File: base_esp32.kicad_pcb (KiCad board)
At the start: 2 copper layers, 100 x 100 mm, 104 parts, among them J1 H_Src_raw, J10 S_IO, J11 H_KEYPAD, J12 S_KEYPAD, J13 BYPASS SRC 5V, J14 BYPASS SRC 3V3, J15 H_SERVO, J16 H_INA1, J17 H_BUZZER, J18 H_INB1, J19 H_IO34, J2 H_5V, J20 H_I2C, J21 S_I2C, J22 H_IO35, J23 H_INA2, J24 H_INB2, J25 H_IO36, J26 H_SPI, J27 S_SPI, J28 DTH11_V1, J29 DTH11_V2, J3 S_5V, J30 H_DTH11, J31 H_DS18B, J32 H_IO39, J33 TX_RX, J34 MOTOR, J35 H_TRIGGER, J36 H_IO33_OUT, J37 H_IO33, J38 ULTRASONIC, J39 H_IO15, J4 H_3V3_2, J40 H_IO15_OUT, J41 H_ECHO, J42 H_IO32, J43 H_IO32_OUT, J44 H_IO02, J45 H_IO02_OUT, J46 H_IO04, J47 H_IO04_OUT, J5 S_3V3_2, J6 H_GND, J7 S_GND, J8 Input Source, J9 H_IO, M1 Servo, SW1 SW_DIP_KEYPAD_1, SW2 SW_DIP_KEYPAD_2, SW3 ENABLE, SW4 INPUT_D1, SW5 SW_DIP_INPUTS, SW6 INPUT_D2, SW7 Selector Input 1, SW8 Selector Input 2, U1 LM7805_TO220, U2 AMS1117, U3 ESP32-DEVKIT-V1, U4 AMS1117, U5 MX1508, U6 DS18B20, U7 LM35-LP

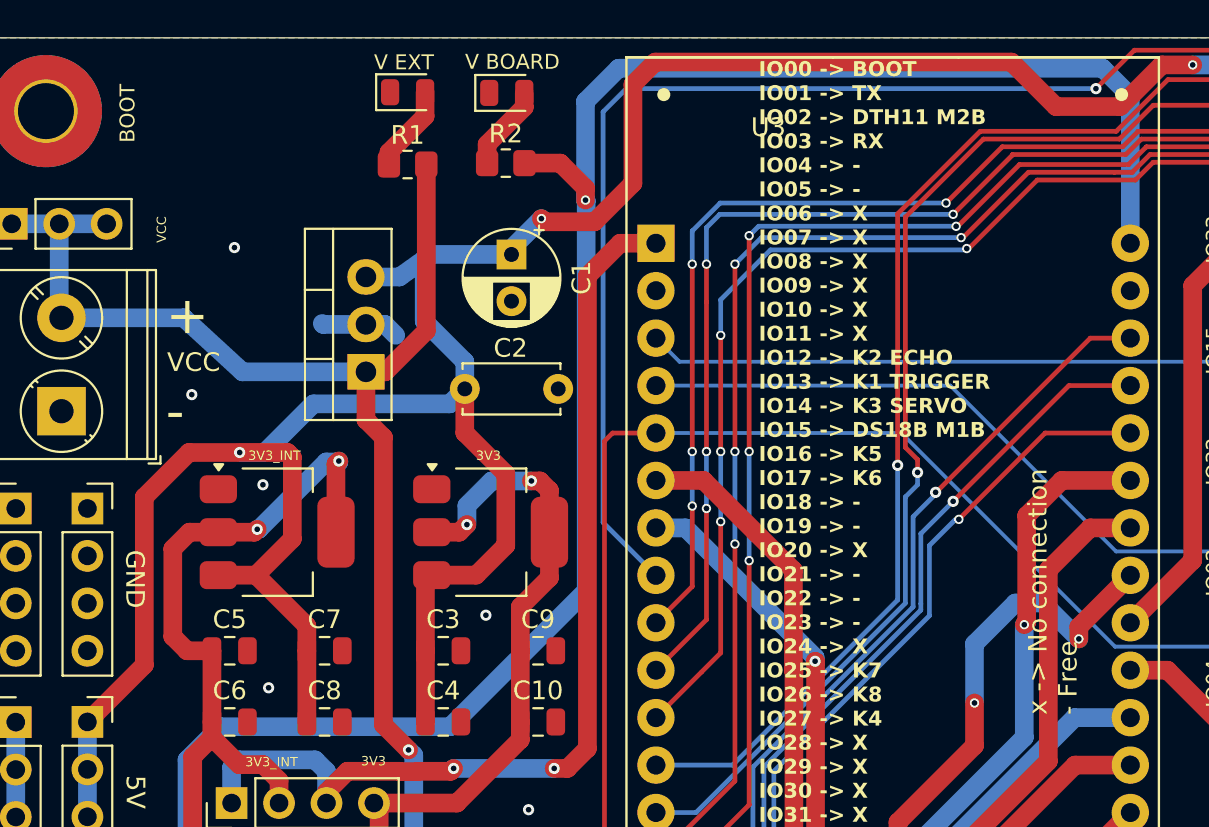
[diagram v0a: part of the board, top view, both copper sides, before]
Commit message: fix: f silkscreen
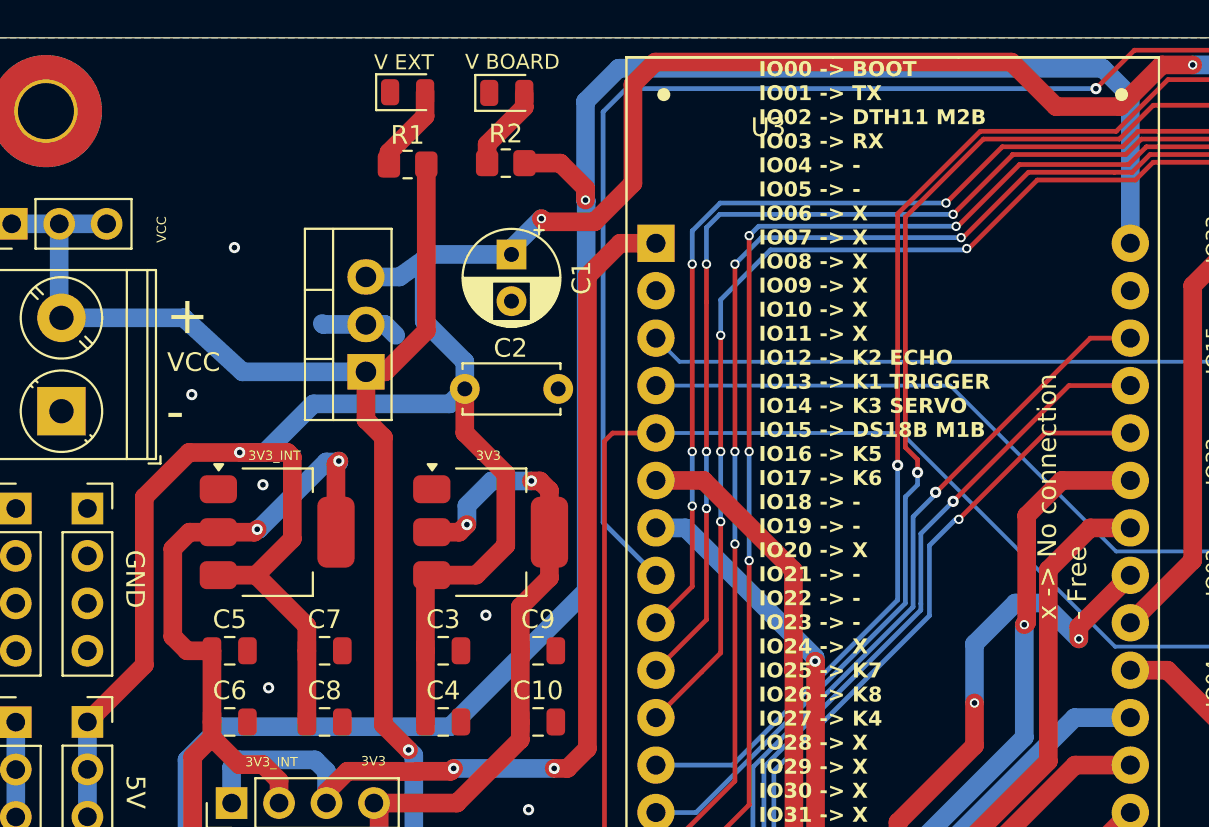
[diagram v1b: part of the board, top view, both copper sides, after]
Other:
- board text removed: "BOOT"
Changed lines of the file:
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@@
 		(pcbplotparams
 			(layerselection 0x00010fc_ffffffff)
-			(plot_on_all_layers_selection 0x0000000_00000000)
+			(plot_on_all_layers_selection 0x0001000_00000000)
 			(disableapertmacros no)
 			(usegerberextensions yes)
@@
 			(sketchpadsonfab no)
 			(subtractmaskfromsilk yes)
-			(outputformat 1)
+			(outputformat 4)
 			(mirror no)
-			(drillshape 0)
+			(drillshape 2)
 			(scaleselection 1)
-			(outputdirectory "gerber/")
+			(outputdirectory "pcb/")
 		)
 	)
@@
 		)
 	)
-	(gr_text "BOOT"
-		(at 118.364 55.499 -0)
-		(layer "B.SilkS")
-		(effects
-			(font
-				(size 0.8 0.8)
-				(thickness 0.1)
-			)
-			(justify left bottom mirror)
-		)
-	)
 	(gr_text "IO16K"
 		(at 135.636 134.0612 90)
@@
 	)
 	(gr_text "x -> No connection\n- Free"
-		(at 142.2908 84.2264 -90)
+		(at 142.494 70.485 -90)
 		(layer "B.SilkS")
 		(effects
@@
 	)
 	(gr_text "x -> No connection\n- Free"
-		(at 162.306 87.249 90)
+		(at 162.814 82.169 90)
 		(layer "F.SilkS")
 		(effects
@@
 			)
 			(justify left bottom)
-		)
-	)
-	(gr_text "BOOT"
-		(at 111.8362 56.6166 90)
-		(layer "F.SilkS")
-		(effects
-			(font
-				(size 0.8 0.8)
-				(thickness 0.1)
-			)
-			(justify left bottom)
